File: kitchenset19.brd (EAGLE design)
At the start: 96.5 x 73.2 mm, 76 parts, among them IC1 AVR-MEGA8-PPTH, J1 POWER_JACKPTH, J2 FTDI Header, Y1 16Mhz

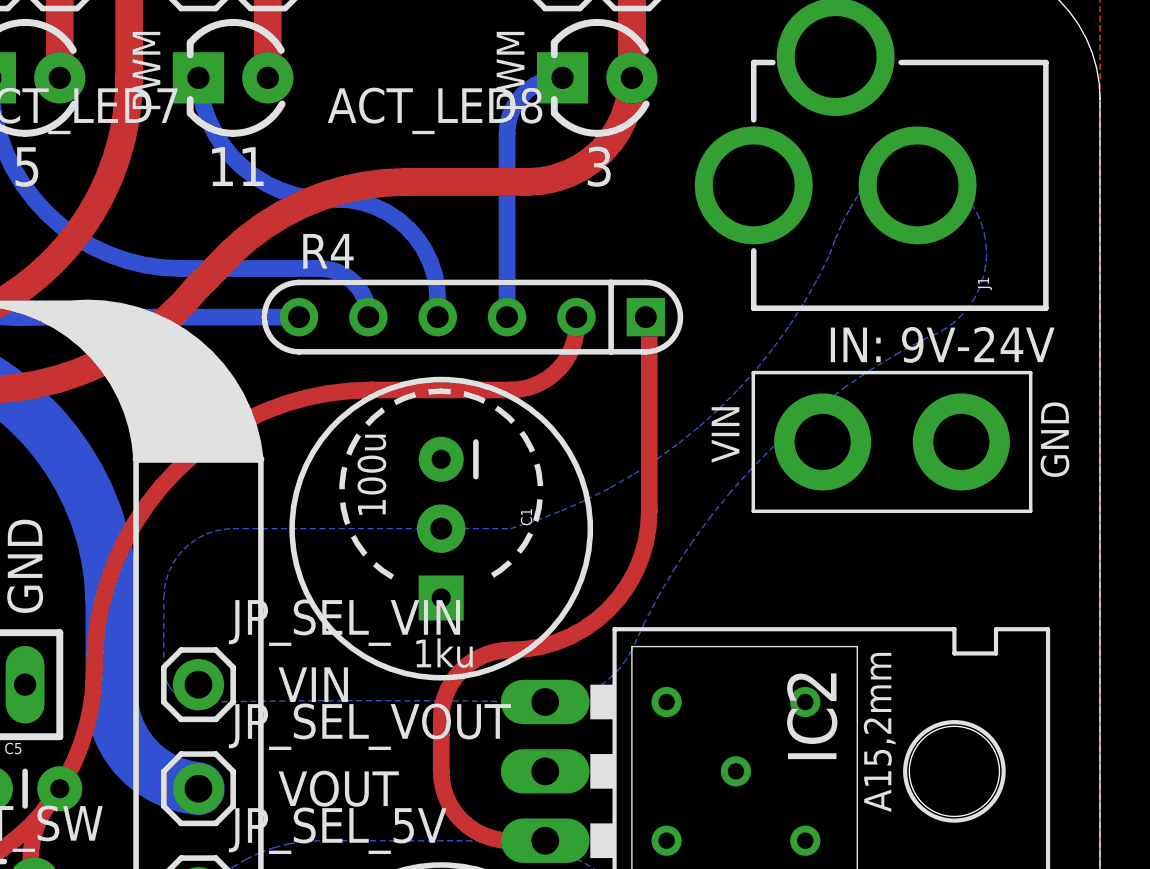
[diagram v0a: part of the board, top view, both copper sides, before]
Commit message: fix incorrect pin assinments on DC barrel jack
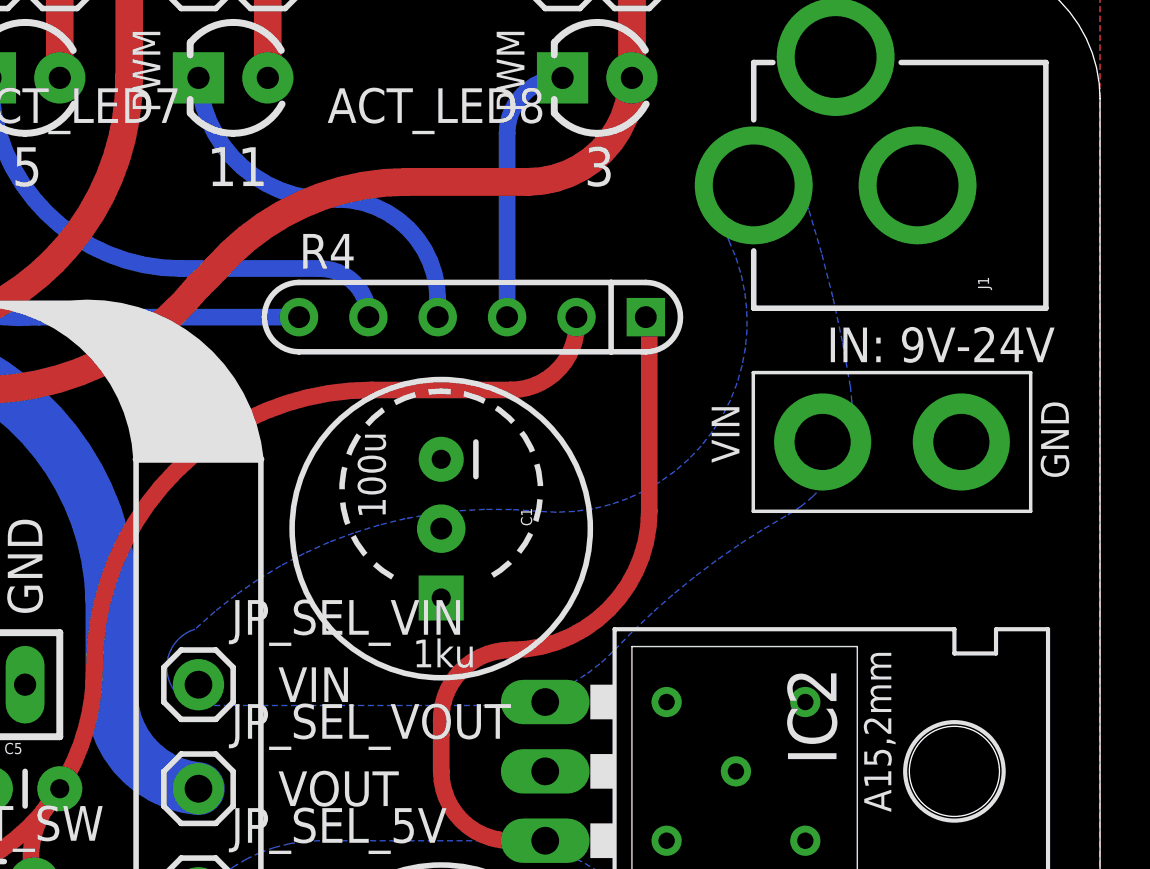
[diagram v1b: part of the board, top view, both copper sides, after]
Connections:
- net GND: now also J1.GND; no longer J1.PWR
- net VIN: now also J1.PWR; no longer J1.GND
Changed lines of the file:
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@@
 <?xml version="1.0" encoding="utf-8"?>
 <!DOCTYPE eagle SYSTEM "eagle.dtd">
-<eagle version="6.2">
+<eagle version="6.4">
 <drawing>
 <settings>
@@
 <setting verticaltext="up"/>
 </settings>
-<grid distance="0.05" unitdist="inch" unit="inch" style="dots" multiple="1" display="no" altdistance="0.025" altunitdist="inch" altunit="inch"/>
+<grid distance="0.05" unitdist="inch" unit="inch" style="dots" multiple="1" display="yes" altdistance="0.005" altunitdist="inch" altunit="inch"/>
 <layers>
 <layer number="1" name="Top" color="4" fill="1" visible="yes" active="yes"/>
@@
 <layer number="19" name="Unrouted" color="6" fill="1" visible="yes" active="yes"/>
 <layer number="20" name="Dimension" color="15" fill="1" visible="yes" active="yes"/>
-<layer number="21" name="tPlace" color="7" fill="1" visible="yes" active="yes"/>
-<layer number="22" name="bPlace" color="7" fill="1" visible="yes" active="yes"/>
+<layer number="21" name="tPlace" color="16" fill="1" visible="yes" active="yes"/>
+<layer number="22" name="bPlace" color="14" fill="1" visible="yes" active="yes"/>
 <layer number="23" name="tOrigins" color="15" fill="1" visible="yes" active="yes"/>
-<layer number="24" name="bOrigins" color="15" fill="1" visible="no" active="yes"/>
+<layer number="24" name="bOrigins" color="15" fill="1" visible="yes" active="yes"/>
 <layer number="25" name="tNames" color="7" fill="1" visible="no" active="yes"/>
 <layer number="26" name="bNames" color="7" fill="1" visible="no" active="yes"/>
@@
 <layer number="43" name="vRestrict" color="2" fill="10" visible="no" active="yes"/>
 <layer number="44" name="Drills" color="7" fill="1" visible="no" active="yes"/>
-<layer number="45" name="Holes" color="7" fill="1" visible="no" active="yes"/>
+<layer number="45" name="Holes" color="7" fill="1" visible="yes" active="yes"/>
 <layer number="46" name="Milling" color="3" fill="1" visible="no" active="yes"/>
 <layer number="47" name="Measures" color="7" fill="1" visible="no" active="yes"/>
@@
 <layer number="49" name="Reference" color="7" fill="1" visible="no" active="yes"/>
 <layer number="50" name="dxf" color="7" fill="1" visible="no" active="no"/>
-<layer number="51" name="tDocu" color="14" fill="1" visible="no" active="yes"/>
+<layer number="51" name="tDocu" color="6" fill="1" visible="yes" active="yes"/>
 <layer number="52" name="bDocu" color="7" fill="1" visible="no" active="yes"/>
 <layer number="53" name="tGND_GNDA" color="7" fill="9" visible="no" active="no"/>
@@
 <layer number="151" name="HeatSink" color="7" fill="1" visible="no" active="yes"/>
 <layer number="200" name="200bmp" color="1" fill="1" visible="no" active="yes"/>
-<layer number="201" name="201bmp" color="7" fill="1" visible="yes" active="yes"/>
+<layer number="201" name="201bmp" color="7" fill="1" visible="no" active="yes"/>
 <layer number="202" name="202bmp" color="14" fill="10" visible="no" active="yes"/>
 <layer number="203" name="203bmp" color="4" fill="10" visible="no" active="yes"/>
@@
 </class>
 </classes>
-<designrules>
+<designrules name="default">
 <description language="en">&lt;b&gt;EAGLE Design Rules&lt;/b&gt;
 &lt;p&gt;
@@
 <contactref element="J2" pad="5"/>
 <contactref element="J2" pad="6"/>
-<contactref element="J1" pad="PWR"/>
 <contactref element="C1" pad="2"/>
 <contactref element="C2" pad="2"/>
 <contactref element="IC1" pad="22"/>
-<contactref element="J1" pad="GNDBREAK"/>
 <contactref element="JPGND" pad="1"/>
 <contactref element="JPGND" pad="2"/>
@@
 <contactref element="R5" pad="P$1"/>
 <contactref element="R2" pad="P$1"/>
+<contactref element="J1" pad="GND"/>
+<contactref element="J1" pad="GNDBREAK"/>
 </signal>
 <signal name="N$4">
@@
 <contactref element="C1" pad="1"/>
 <contactref element="JP_SEL_VIN" pad="1"/>
-<contactref element="J1" pad="GND"/>
-<polygon width="1.778" layer="16" isolate="0.6096">
-<vertex x="62.23" y="36.83"/>
-<vertex x="62.23" y="39.37" curve="-90"/>
-<vertex x="64.77" y="41.91"/>
-<vertex x="74.93" y="41.91" curve="48.88791"/>
-<vertex x="86.614" y="51.943" curve="-22.025856"/>
-<vertex x="88.392" y="55.118" curve="-31.104245"/>
-<vertex x="89.535" y="55.245" curve="-152.591143"/>
-<vertex x="90.17" y="48.895" curve="39.716673"/>
-<vertex x="79.375" y="37.465" curve="-63.839342"/>
-<vertex x="76.2" y="35.56" curve="1.911743"/>
-<vertex x="63.5" y="35.56" curve="-91.914841"/>
-</polygon>
 <contactref element="JPSUPPLY" pad="2"/>
 <via x="72.39" y="41.91" extent="1-16" drill="0.8" diameter="1.778" shape="square"/>
+<contactref element="J1" pad="PWR"/>
+<polygon width="1.27" layer="16">
+<vertex x="63.373" y="35.433"/>
+<vertex x="74.041" y="35.433" curve="46.770442"/>
+<vertex x="78.74" y="37.465" curve="-17.632421"/>
+<vertex x="85.09" y="42.418" curve="69.839336"/>
+<vertex x="87.376" y="47.117" curve="8.526345"/>
+<vertex x="85.852" y="53.594" curve="187.733945"/>
+<vertex x="82.931" y="52.451" curve="-120.852577"/>
+<vertex x="75.946" y="42.545" curve="49.13851"/>
+<vertex x="63.373" y="38.227" curve="146.083155"/>
+</polygon>
 </signal>
 <signal name="N$33">
